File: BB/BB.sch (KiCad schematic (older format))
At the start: 234 parts, among them SW0 SW_Push, U1 AT90USB1286-AU, Y0 16Mhz

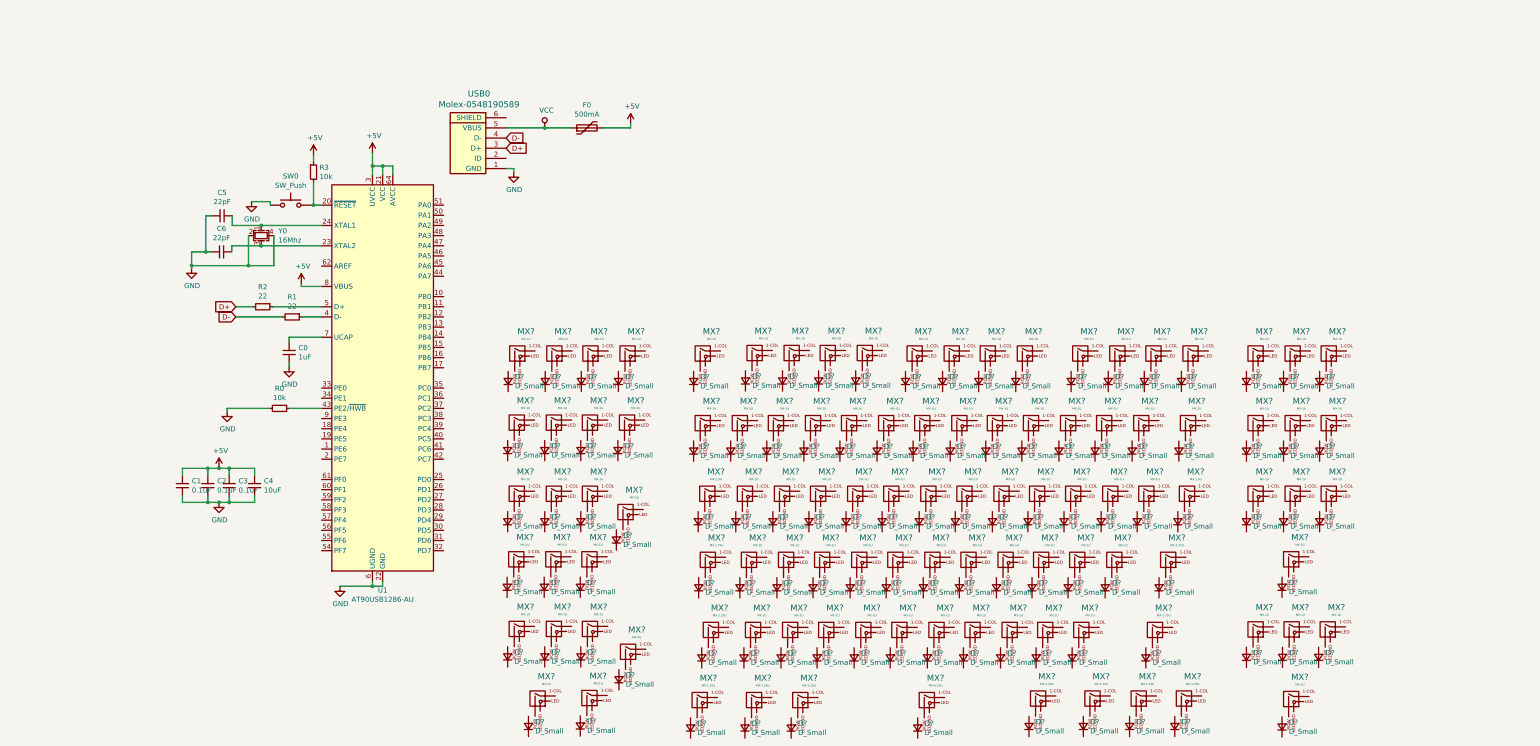
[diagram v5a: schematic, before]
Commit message: Columns Wired
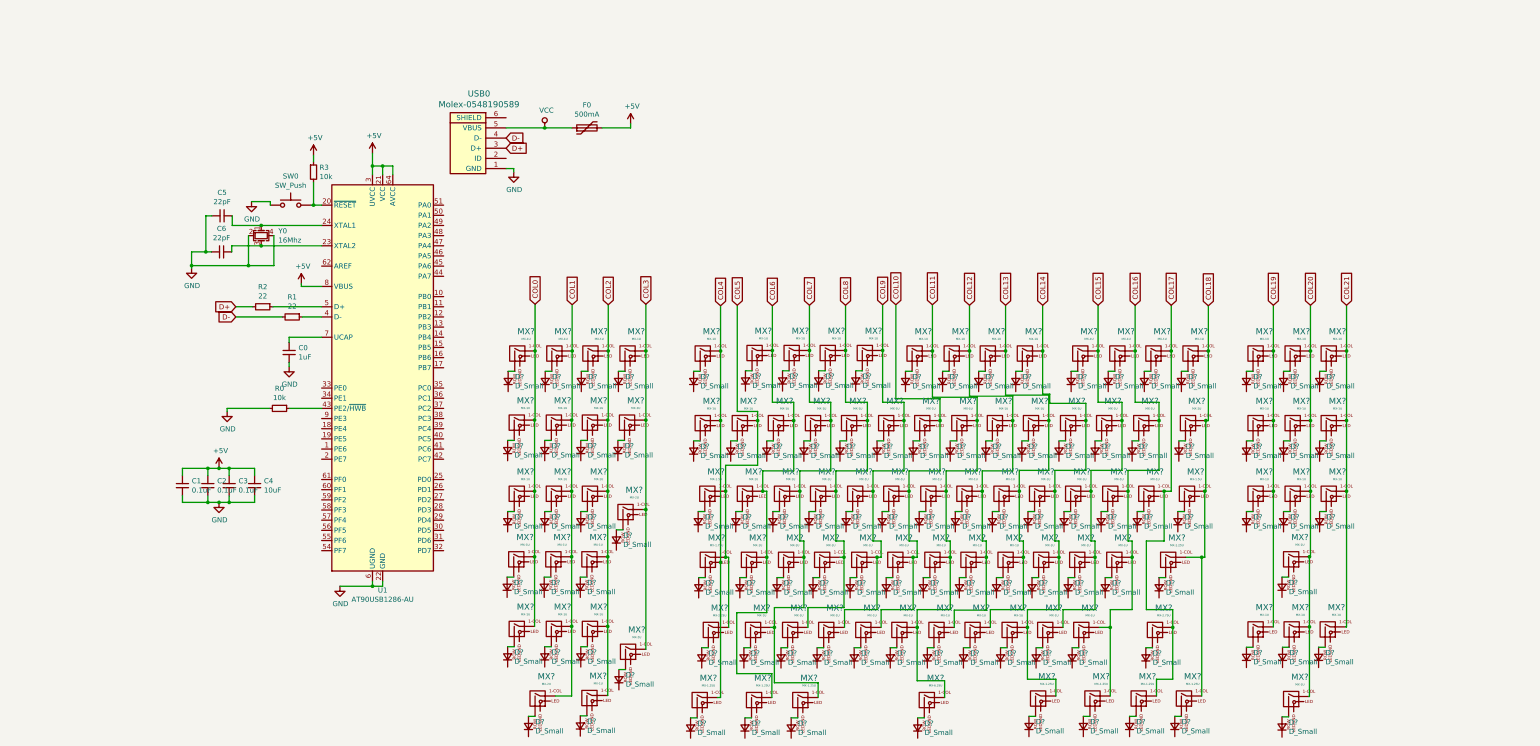
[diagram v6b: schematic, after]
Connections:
- net COL0: now reaches MX?.1 (COL)
- net COL0: now also MX?.1 (COL), MX?.1 (COL), MX?.1 (COL), MX?.1 (COL)
- net at MX?.2 (ROW): now also D?.2 (A) (x109)
- net COL1: now reaches MX?.1 (COL)
- net COL1: now also MX?.1 (COL), MX?.1 (COL), MX?.1 (COL), MX?.1 (COL), MX?.1 (COL)
- net COL2: now reaches MX?.1 (COL)
- net COL2: now also MX?.1 (COL), MX?.1 (COL), MX?.1 (COL), MX?.1 (COL), MX?.1 (COL)
- net COL3: now reaches MX?.1 (COL)
- net COL3: now also MX?.1 (COL), MX?.1 (COL), MX?.1 (COL)
- net COL4: now reaches MX?.1 (COL)
- net COL4: now also MX?.1 (COL), MX?.1 (COL), MX?.3 (LED)
- net COL6: now reaches MX?.1 (COL)
- net COL6: now also MX?.1 (COL), MX?.1 (COL), MX?.1 (COL), MX?.1 (COL)
- net COL7: now reaches MX?.1 (COL)
- net COL7: now also MX?.1 (COL), MX?.1 (COL), MX?.1 (COL), MX?.1 (COL), MX?.1 (COL)
- net COL8: now reaches MX?.1 (COL)
- net COL8: now also MX?.1 (COL), MX?.1 (COL), MX?.1 (COL), MX?.1 (COL)
- net COL9: now reaches MX?.1 (COL)
- net COL9: now also MX?.1 (COL), MX?.1 (COL), MX?.1 (COL)
- net COL11: now reaches MX?.1 (COL)
- net COL11: now also MX?.1 (COL), MX?.1 (COL), MX?.1 (COL), MX?.1 (COL), MX?.1 (COL)
- net COL12: now reaches MX?.1 (COL)
- net COL12: now also MX?.1 (COL), MX?.1 (COL), MX?.1 (COL), MX?.1 (COL)
- net COL13: now reaches MX?.1 (COL)
- net COL13: now also MX?.1 (COL), MX?.1 (COL), MX?.1 (COL), MX?.1 (COL)
- net COL14: now reaches MX?.1 (COL)
- net COL14: now also MX?.1 (COL), MX?.1 (COL), MX?.1 (COL), MX?.1 (COL), MX?.1 (COL)
- net COL15: now reaches MX?.1 (COL)
- net COL15: now also MX?.1 (COL), MX?.1 (COL), MX?.1 (COL), MX?.1 (COL)
- net COL16: now reaches MX?.1 (COL)
- net COL16: now also MX?.1 (COL), MX?.1 (COL), MX?.1 (COL), MX?.1 (COL), MX?.1 (COL)
- net COL17: now reaches MX?.1 (COL)
- net COL17: now also MX?.1 (COL), MX?.1 (COL), MX?.1 (COL)
- net COL18: now reaches MX?.1 (COL)
- net COL18: now also MX?.1 (COL), MX?.1 (COL), MX?.1 (COL), MX?.1 (COL)
- net COL19: now reaches MX?.1 (COL)
- net COL19: now also MX?.1 (COL), MX?.1 (COL), MX?.1 (COL)
- net COL20: now reaches MX?.1 (COL)
- net COL20: now also MX?.1 (COL), MX?.1 (COL), MX?.1 (COL), MX?.1 (COL), MX?.1 (COL)
- net COL21: now reaches MX?.1 (COL)
- net COL21: now also MX?.1 (COL), MX?.1 (COL), MX?.1 (COL)
- net COL5: now reaches MX?.1 (COL)
- net COL5: now also MX?.1 (COL), MX?.1 (COL), MX?.1 (COL)
- net COL10: now reaches MX?.1 (COL)
- net COL10: now also MX?.1 (COL), MX?.1 (COL), MX?.1 (COL)

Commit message: Rows and Columns Connected Up
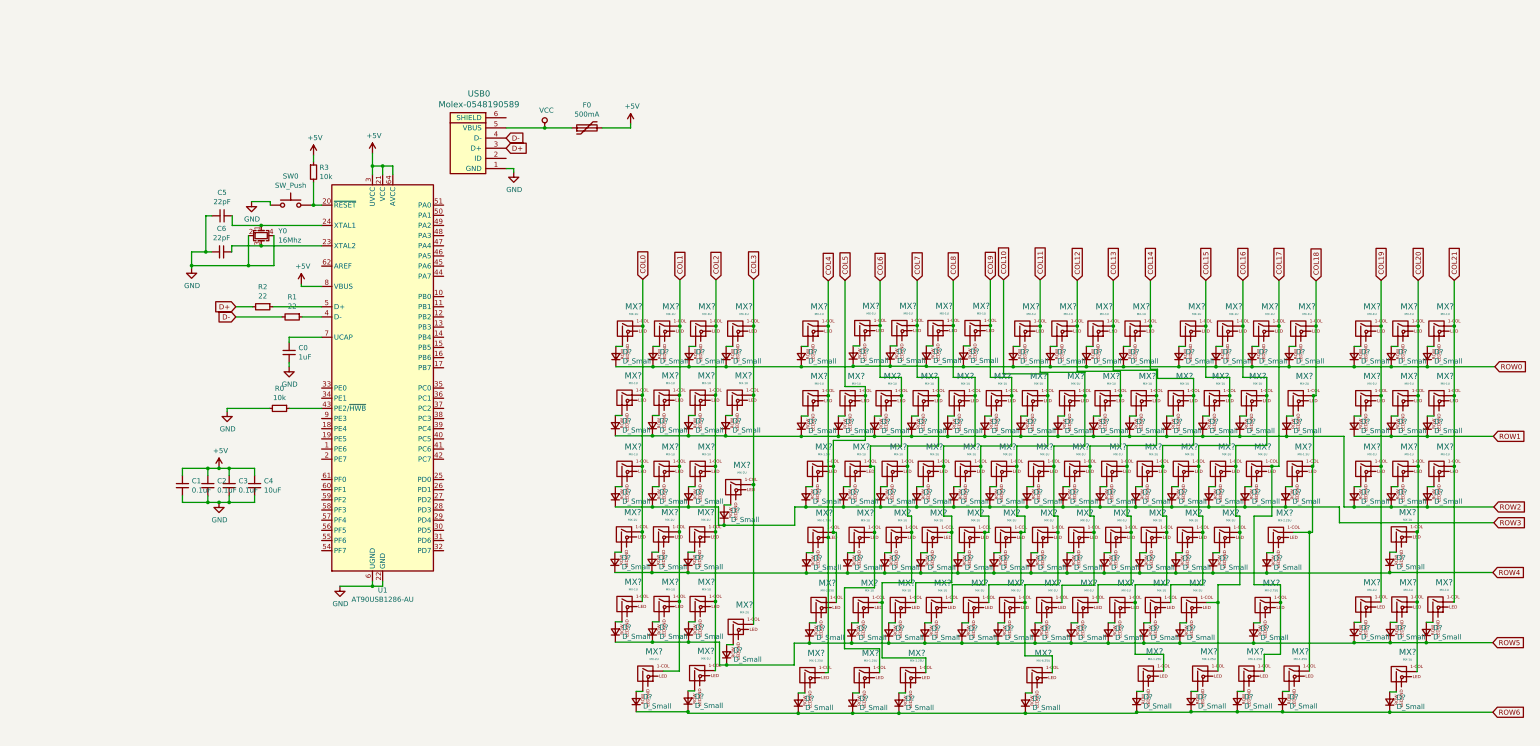
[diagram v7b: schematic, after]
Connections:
- net ROW0: now reaches D?.1 (K)
- net ROW0: now also D?.1 (K), D?.1 (K), D?.1 (K), D?.1 (K), D?.1 (K), D?.1 (K), D?.1 (K), D?.1 (K), D?.1 (K), D?.1 (K), D?.1 (K), D?.1 (K), D?.1 (K), D?.1 (K), D?.1 (K), D?.1 (K), D?.1 (K), D?.1 (K), D?.1 (K)
- net ROW2: now reaches D?.1 (K)
- net ROW2: now also D?.1 (K), D?.1 (K), D?.1 (K), D?.1 (K), D?.1 (K), D?.1 (K), D?.1 (K), D?.1 (K), D?.1 (K), D?.1 (K), D?.1 (K), D?.1 (K), D?.1 (K), D?.1 (K), D?.1 (K), D?.1 (K), D?.1 (K), D?.1 (K), D?.1 (K), D?.1 (K)
- net ROW3: now reaches D?.1 (K)
- net ROW3: now also D?.1 (K), D?.1 (K), D?.1 (K), D?.1 (K), D?.1 (K), D?.1 (K), D?.1 (K), D?.1 (K), D?.1 (K), D?.1 (K), D?.1 (K), D?.1 (K), D?.1 (K), D?.1 (K), D?.1 (K), D?.1 (K), D?.1 (K)
- net ROW4: now reaches D?.1 (K)
- net ROW4: now also D?.1 (K), D?.1 (K), D?.1 (K), D?.1 (K), D?.1 (K), D?.1 (K), D?.1 (K), D?.1 (K), D?.1 (K), D?.1 (K), D?.1 (K), D?.1 (K), D?.1 (K), D?.1 (K), D?.1 (K), D?.1 (K)
- net ROW5: now reaches D?.1 (K)
- net ROW5: now also D?.1 (K), D?.1 (K), D?.1 (K), D?.1 (K), D?.1 (K), D?.1 (K), D?.1 (K), D?.1 (K), D?.1 (K), D?.1 (K), D?.1 (K), D?.1 (K), D?.1 (K), D?.1 (K), D?.1 (K), D?.1 (K), D?.1 (K), D?.1 (K)
- net ROW6: now reaches D?.1 (K)
- net ROW6: now also D?.1 (K), D?.1 (K), D?.1 (K), D?.1 (K), D?.1 (K), D?.1 (K), D?.1 (K), D?.1 (K), D?.1 (K), D?.1 (K)
- net ROW1: now reaches D?.1 (K)
- net ROW1: now also D?.1 (K), D?.1 (K)
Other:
- moved on the sheet: D?, MX?

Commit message: Finished Schematic
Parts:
- C0, C1, C2, C3, C4, C5, C6: footprint (none) -> Capacitor_SMD:C_0805_2012Metric
- D1, D10, D100, D101, D102, D103, D104, D105, D106, D107, D108, D109, D11, D12, D13, D14, D15, D16, D17, D18, D19, D2, D20, D21, D22, D23, D24, D25, D26, D27, D28, D29, D3, D30, D31, D32, D33, D34, D35, D36, D37, D38, D39, D4, D40, D41, D42, D43, D44, D45, D46, D47, D48, D49, D5, D50, D51, D52, D53, D54, D55, D56, D57, D58, D59, D6, D60, D61, D62, D63, D64, D65, D66, D67, D68, D69, D7, D70, D71, D72, D73, D74, D75, D76, D77, D78, D79, D8, D80, D81, D82, D83, D84, D85, D86, D87, D88, D89, D9, D90, D91, D92, D93, D94, D95, D96, D97, D98, D99: renamed from D?; footprint (none) -> Diode_SMD:D_SOD-123
- F0: footprint (none) -> Fuse:Fuse_1206_3216Metric
- MX1, MX10, MX105, MX11, MX12, MX13, MX14, MX15, MX16, MX17, MX18, MX19, MX2, MX20, MX21, MX22, MX23, MX24, MX25, MX26, MX27, MX28, MX29, MX3, MX30, MX31, MX32, MX33, MX34, MX35, MX36, MX37, MX38, MX39, MX4, MX40, MX41, MX42, MX43, MX44, MX46, MX47, MX48, MX49, MX5, MX50, MX51, MX52, MX53, MX54, MX55, MX56, MX57, MX59, MX6, MX60, MX61, MX62, MX63, MX64, MX65, MX66, MX68, MX69, MX7, MX70, MX71, MX72, MX73, MX74, MX75, MX76, MX77, MX78, MX8, MX80, MX81, MX82, MX83, MX84, MX85, MX87, MX88, MX89, MX9, MX90, MX91, MX92, MX93, MX94, MX95, MX96, MX99: renamed from MX?; footprint (none) -> MX_Alps_Hybrid:MX-1U
- MX100, MX98: renamed from MX?; footprint (none) -> MX_Alps_Hybrid:MX-2U
- MX101, MX102, MX103, MX104, MX106, MX107, MX108: renamed from MX?; footprint (none) -> MX_Alps_Hybrid:MX-1.25U
- MX109: renamed from MX?; footprint (none) -> MX_Alps_Hybrid:MX-6.25U
- MX45, MX58: renamed from MX?; footprint (none) -> MX_Alps_Hybrid:MX-1.5U
- MX67: renamed from MX?; footprint (none) -> MX_Alps_Hybrid:MX-1.75U
- MX79, MX86: renamed from MX?; footprint (none) -> MX_Alps_Hybrid:MX-2.25U
- MX97: renamed from MX?; footprint (none) -> MX_Alps_Hybrid:MX-2.75U
- R0, R1, R2, R3: footprint (none) -> Resistor_SMD:R_0805_2012Metric
- SW0: footprint (none) -> random-keyboard-parts:SKQG-1155865
- USB0: footprint (none) -> random-keyboard-parts:Molex-0548190589
- Y0: footprint (none) -> Crystal:Crystal_SMD_3225-4Pin_3.2x2.5mm
